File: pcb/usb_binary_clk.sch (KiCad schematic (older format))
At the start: 45 parts, among them J1 USB_B_Micro, J2 USB_B_Micro, J3 AVR-ISP-6, SW1 SW_Push, SW2 SW_Push, SW3 SW_Push, U1 MCP7940N-xP, U2 ATtiny84V-10PU, Y1 Crystal

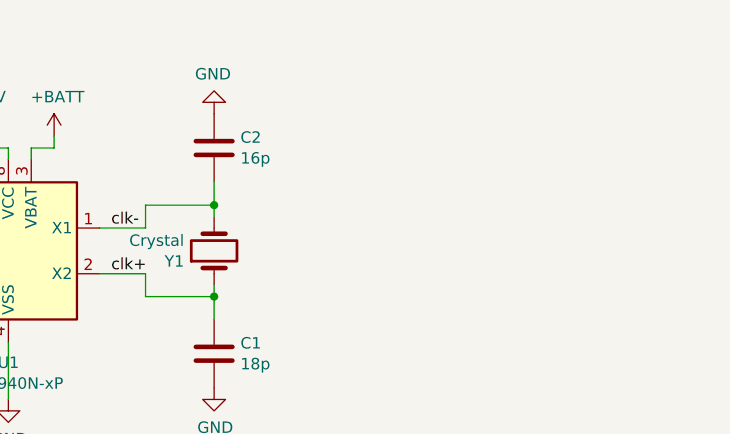
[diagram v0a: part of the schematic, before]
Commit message: add notes in schematic
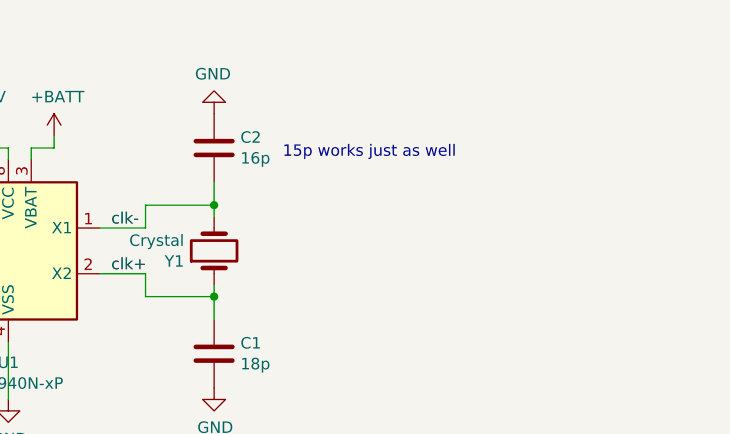
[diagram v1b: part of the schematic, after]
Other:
- note added: "15p works just as well"
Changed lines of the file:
@@
 encoding utf-8
 Sheet 1 1
-Title ""
-Date ""
-Rev ""
-Comp ""
+Title "Binary Clock"
+Date "2022-08-05"
+Rev "1"
+Comp "UNIKAT Ilmenau"
 Comment1 ""
 Comment2 ""
@@
 Text Notes 5550 6050 0    50   ~ 0
 Mounting pads
+Text Notes 8850 1400 0    50   ~ 0
+15p works just as well
 $EndSCHEMATC
